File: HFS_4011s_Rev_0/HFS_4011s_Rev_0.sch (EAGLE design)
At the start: 15 parts, among them IC1 CP2104, J1 2X06, J2 2X12, Q1 mmbt2222, Q2 mmbt2222, SW2 KMR2, X2 ESP32_WROOM32_SKINNY, X4 20329

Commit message: Added power circuitry to board. Using 5V buck boost and 3.3V LDO. Added 1x02 pin header for on-off switch.
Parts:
- added B1: 1.8-5V, microbuilder:BATTERY
- added C1: 10uF, microbuilder:CAP_CERAMIC0805-NOOUTLINE
- added C3: 2.2uF, microbuilder:CAP_CERAMIC0805-NOOUTLINE
- added C5: 0.1uF, microbuilder:CAP_CERAMIC0805-NOOUTLINE
- added C6: 10µF, microbuilder:CAP_CERAMIC0805-NOOUTLINE
- added C7: 100uF/6V, microbuilder:CAP_TANTALUMB/3528_REFLOW
- added C8: 0.47uF, microbuilder:CAP_CERAMIC0603_NO
- added C9: 33uF, microbuilder:CAP_CERAMIC0603_NO
- added J3: 1X02, HFS4011sCustom:1X02
- added L1: VLC5045-6.8uH, microbuilder:INDUCTORTDK_VLC5045
- added LBO: RED, microbuilder:LED0805_NOOUTLINE
- added LED3: ORANGE, microbuilder:LED0805_NOOUTLINE
- added LED4: GREEN, microbuilder:LED0805_NOOUTLINE
- added PWR: BLUE, microbuilder:LED0805_NOOUTLINE
- added Q3: MMUN2133LT1G, transistor:MUN2114T1-PNP_DRIVER-SC59-BEC
- added R11, R2: 340K, microbuilder:RESISTOR0805_NOOUTLINE
- added R12, R4: 1.87Mohm, microbuilder:RESISTOR0805_NOOUTLINE
- added R20, R5, R7: 1K, microbuilder:RESISTOR0805_NOOUTLINE
- added R6: 470, microbuilder:RESISTOR0805_NOOUTLINE
- added R8: 2k, microbuilder:RESISTOR0805_NOOUTLINE
- added R9: 200K, microbuilder:RESISTOR0805_NOOUTLINE
- added U1: TPS61090RSAR, microbuilder:VREG_TPS6103X
- added U2: MCP73831T-2ACI/OT, microbuilder:MCP73831/2
- added U3: LM3940, HFS4011sCustom:LM3940
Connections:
- new net 5.0V: C3.1, C7.+, C8.1, PWR.A, R4.2, U1.VOUT, U3.IN
- new net ENABLE: J3.1, R2.2, U1.EN
- new net LBO: Q3.B, U1.LBO
- new net N$1: LED3.C, R6.1
- new net N$10: PWR.C, R5.1
- new net N$11: R4.1, R9.2, U1.FB
- new net N$14: LBO.A, R20.1
- new net N$15: Q3.C, R20.2
- new net N$3: L1.2, U1.SW
- new net N$4: R11.2, R12.1, U1.LBI
- new net N$7: R6.2, R7.2, U2.STAT
- new net N$8: R8.1, U2.PROG
- new net N$9: LED4.A, R7.1
- net 3.3V: now also C9.1, U3.OUT
- net GND: now also B1.-, C1.2, C3.2, C5.2, C6.2, C7.-, C8.2, C9.2, J3.2, LBO.C, LED4.C, R11.1, R5.2, R8.2, R9.1, U1.GND, U1.PGND, U1.SYNC, U2.VSS, U3.GND
- net VBAT: now also B1.+, C1.1, C5.1, L1.1, Q3.E, R12.2, R2.1, U1.VBAT, U2.VBAT
- net VBUS: now also C6.1, LED3.A, U2.VDD
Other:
- note added: "2.0K = 500mA"
- note added: "6.8uH power w/2A current"
- note added: "R2 < 500K R1 = 5.5*R2 (3.2V LBO)"
- note added: "R4 = 200K R3 = 1.85Mohm"
- note added: "See Pg 15 1st para"

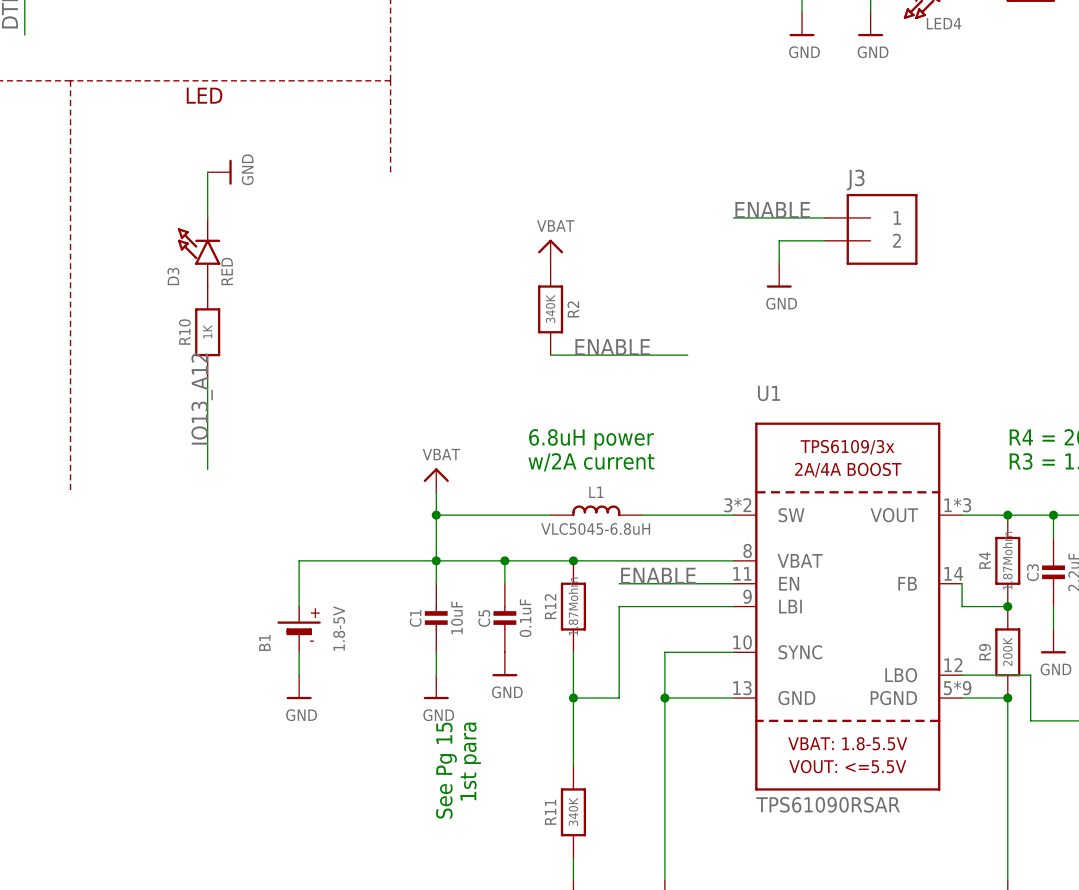
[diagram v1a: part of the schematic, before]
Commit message: Added TVS diode on battery, and moved switch to battery.
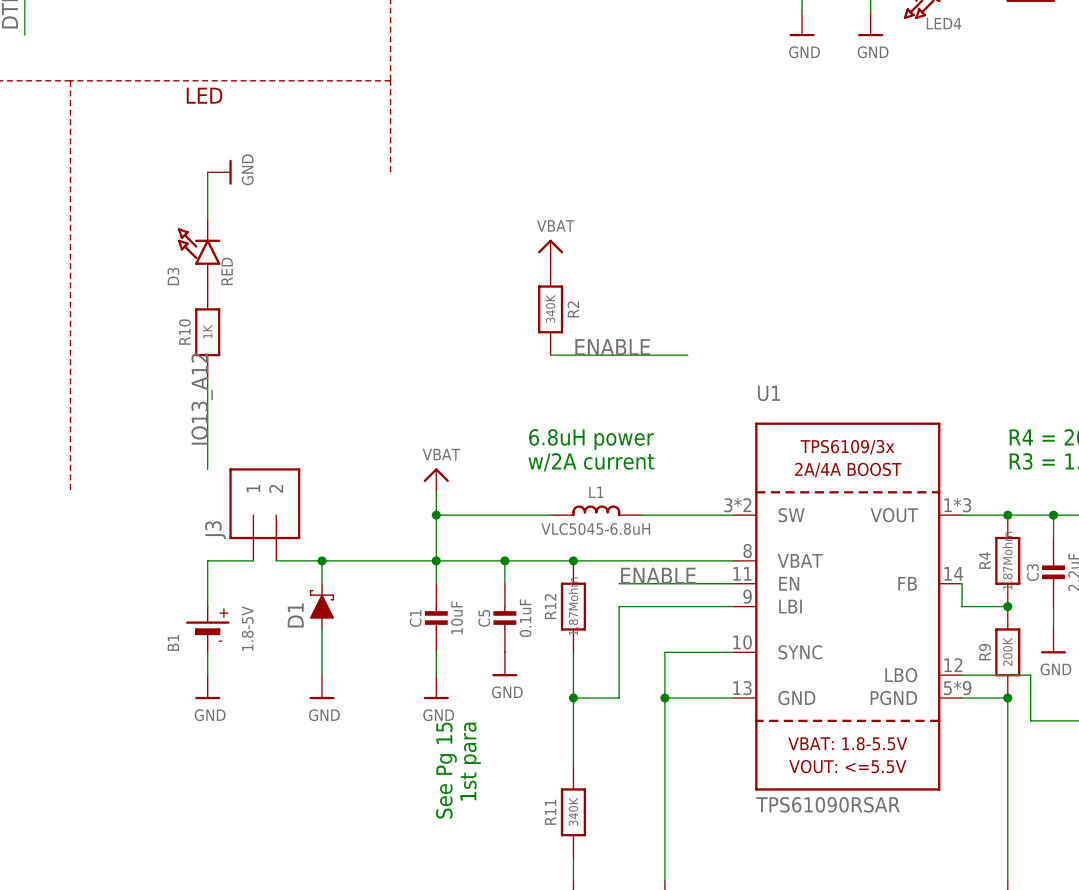
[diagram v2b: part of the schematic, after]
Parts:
- added D1: SMAJ5.0CALFDKR-ND, HFS4011sCustom:SMAJ5.0CALFDKR-ND
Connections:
- new net N$16: B1.+, J3.1
- net ENABLE: no longer J3.1
- net GND: now also D1.A; no longer J3.2
- net VBAT: now also D1.C, J3.2; no longer B1.+
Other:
- moved on the sheet: B1, J3
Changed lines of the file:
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@@
 <part name="Q3" library="transistor" deviceset="*-PNP_DRIVER-" device="SC59-BEC" technology="MUN2114T1" value="MMUN2133LT1G"/>
 <part name="J3" library="HFS4011sCustom" deviceset="1X02" device=""/>
-<part name="U$16" library="microbuilder" deviceset="GND" device=""/>
 <part name="U3" library="HFS4011sCustom" deviceset="LM3940" device=""/>
 <part name="U$23" library="microbuilder" deviceset="GND" device=""/>
@@
 <part name="U$30" library="microbuilder" deviceset="GND" device=""/>
 <part name="U$35" library="microbuilder" deviceset="3.3V" device=""/>
+<part name="D1" library="HFS4011sCustom" deviceset="SMAJ5.0CALFDKR-ND" device=""/>
+<part name="U$16" library="microbuilder" deviceset="GND" device=""/>
 </parts>
 <sheets>
@@
 <instance part="C1" gate="G$1" x="154.94" y="53.34"/>
 <instance part="U$6" gate="G$1" x="154.94" y="45.72"/>
-<instance part="B1" gate="G$1" x="139.7" y="53.34" rot="R90"/>
-<instance part="U$7" gate="G$1" x="139.7" y="45.72"/>
+<instance part="B1" gate="G$1" x="129.54" y="53.34" rot="R90"/>
+<instance part="U$7" gate="G$1" x="129.54" y="45.72"/>
 <instance part="C3" gate="G$1" x="223.52" y="58.42"/>
 <instance part="U$9" gate="G$1" x="241.3" y="88.9"/>
@@
 <attribute name="VALUE" x="259.08" y="40.64" size="1.778" layer="96"/>
 </instance>
-<instance part="J3" gate="G$1" x="203.2" y="96.52"/>
-<instance part="U$16" gate="G$1" x="193.04" y="91.44"/>
+<instance part="J3" gate="G$1" x="137.16" y="66.04" rot="R90"/>
 <instance part="U3" gate="G$1" x="294.64" y="83.82"/>
 <instance part="U$23" gate="G$1" x="289.56" y="76.2"/>
@@
 <instance part="U$30" gate="G$1" x="284.48" y="68.58"/>
 <instance part="U$35" gate="G$1" x="284.48" y="88.9"/>
+<instance part="D1" gate="G$1" x="142.24" y="55.88" rot="R90"/>
+<instance part="U$16" gate="G$1" x="142.24" y="45.72"/>
 </instances>
 <busses>
@@
 <pinref part="B1" gate="G$1" pin="-"/>
 <pinref part="U$7" gate="G$1" pin="GND"/>
-<wire x1="139.7" y1="50.8" x2="139.7" y2="48.26" width="0.1524" layer="91"/>
+<wire x1="129.54" y1="50.8" x2="129.54" y2="48.26" width="0.1524" layer="91"/>
 </segment>
 <segment>
@@
 </segment>
 <segment>
-<pinref part="J3" gate="G$1" pin="2"/>
-<wire x1="198.12" y1="96.52" x2="193.04" y2="96.52" width="0.1524" layer="91"/>
-<pinref part="U$16" gate="G$1" pin="GND"/>
-<wire x1="193.04" y1="93.98" x2="193.04" y2="96.52" width="0.1524" layer="91"/>
-</segment>
-<segment>
 <pinref part="C8" gate="G$1" pin="2"/>
 <pinref part="U$29" gate="G$1" pin="GND"/>
@@
 <pinref part="C9" gate="G$1" pin="2"/>
 <wire x1="284.48" y1="71.12" x2="284.48" y2="73.66" width="0.1524" layer="91"/>
+</segment>
+<segment>
+<pinref part="D1" gate="G$1" pin="A"/>
+<pinref part="U$16" gate="G$1" pin="GND"/>
+<wire x1="142.24" y1="53.34" x2="142.24" y2="48.26" width="0.1524" layer="91"/>
 </segment>
 </net>
@@
 <pinref part="R12" gate="G$1" pin="2"/>
 <junction x="170.18" y="60.96"/>
-<pinref part="B1" gate="G$1" pin="+"/>
-<wire x1="139.7" y1="60.96" x2="139.7" y2="55.88" width="0.1524" layer="91"/>
-<wire x1="139.7" y1="60.96" x2="154.94" y2="60.96" width="0.1524" layer="91"/>
+<pinref part="J3" gate="G$1" pin="2"/>
+<pinref part="D1" gate="G$1" pin="C"/>
+<wire x1="137.16" y1="60.96" x2="142.24" y2="60.96" width="0.1524" layer="91"/>
+<wire x1="142.24" y1="60.96" x2="142.24" y2="58.42" width="0.1524" layer="91"/>
+<wire x1="142.24" y1="60.96" x2="154.94" y2="60.96" width="0.1524" layer="91"/>
+<junction x="142.24" y="60.96"/>
 </segment>
 <segment>
@@
 <label x="175.26" y="58.42" size="1.778" layer="95"/>
 </segment>
-<segment>
-<pinref part="J3" gate="G$1" pin="1"/>
-<wire x1="198.12" y1="99.06" x2="187.96" y2="99.06" width="0.1524" layer="91"/>
-<label x="187.96" y="99.06" size="1.778" layer="95"/>
-</segment>
 </net>
 <net name="N$11" class="0">
@@
 </segment>
 </net>
+<net name="N$16" class="0">
+<segment>
+<pinref part="B1" gate="G$1" pin="+"/>
+<wire x1="129.54" y1="60.96" x2="129.54" y2="55.88" width="0.1524" layer="91"/>
+<pinref part="J3" gate="G$1" pin="1"/>
+<wire x1="129.54" y1="60.96" x2="134.62" y2="60.96" width="0.1524" layer="91"/>
+</segment>
+</net>

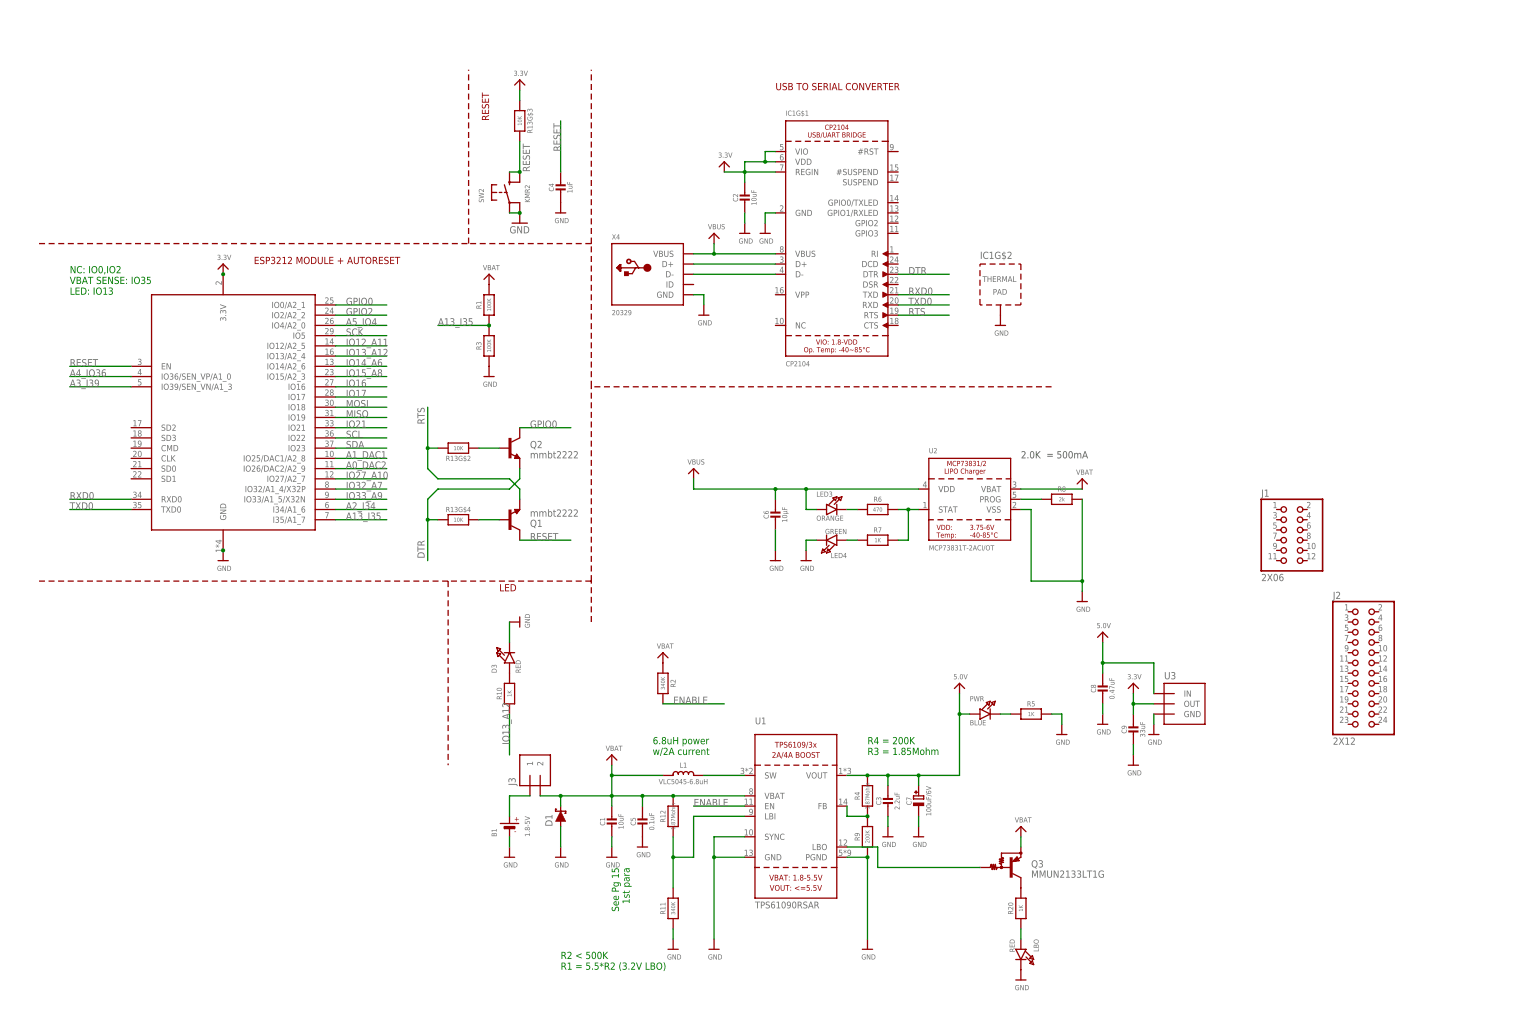
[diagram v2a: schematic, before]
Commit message: Cleaned up schematic and added ground planes.
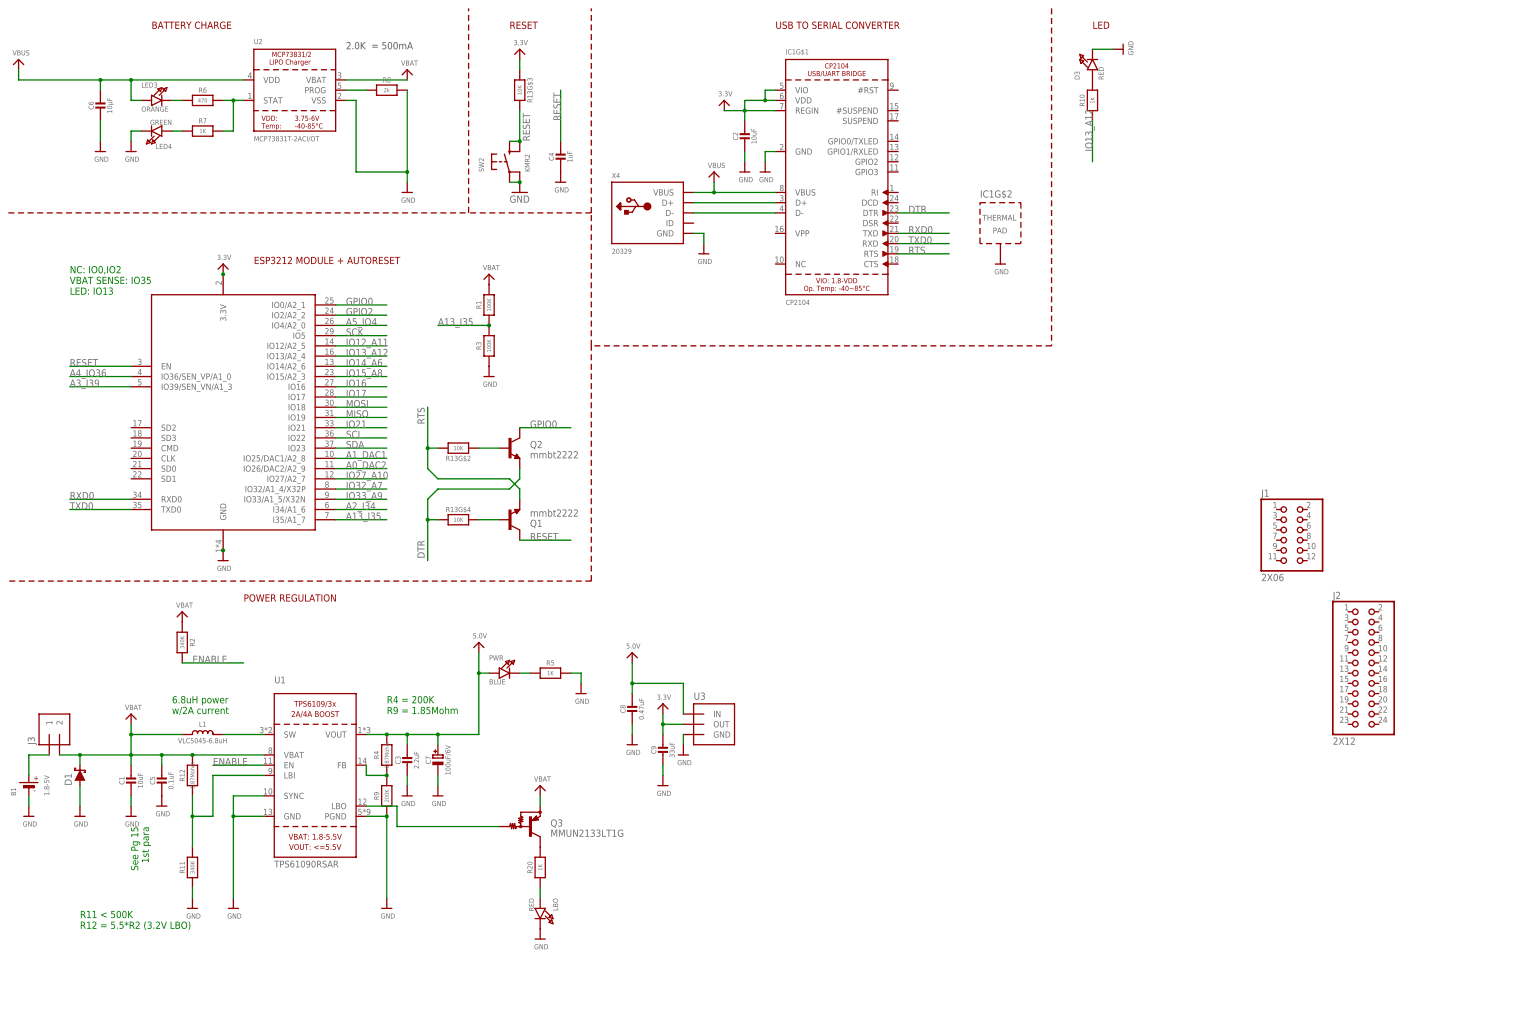
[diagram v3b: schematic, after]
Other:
- note added: "BATTERY CHARGE"
- note added: "POWER REGULATION"
- note added: "R11 < 500K R12 = 5.5*R2 (3.2V LBO)"
- note added: "R4 = 200K R9 = 1.85Mohm"
- note removed: "R2 < 500K R1 = 5.5*R2 (3.2V LBO)"
- note removed: "R4 = 200K R3 = 1.85Mohm"
- moved on the sheet: B1, C1, C2, C3, C4, C5, C6, C7, C8, C9, D1, D3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
